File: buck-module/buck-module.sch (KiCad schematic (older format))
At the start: 10 parts, among them P1 CONN_01X04, P2 CONN_01X02, U1 ADP2301

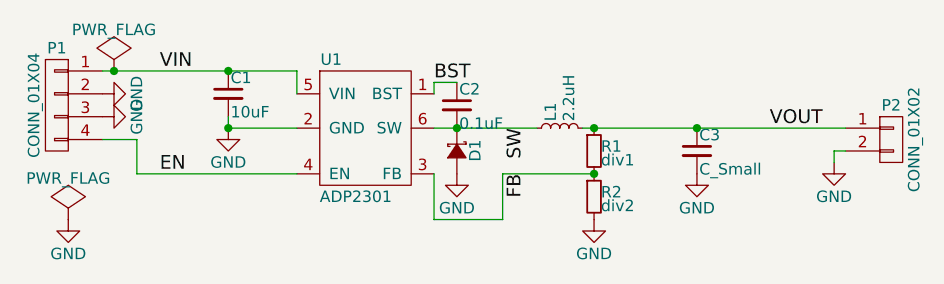
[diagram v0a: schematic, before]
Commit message: Fill in last details for power supply, cleanup
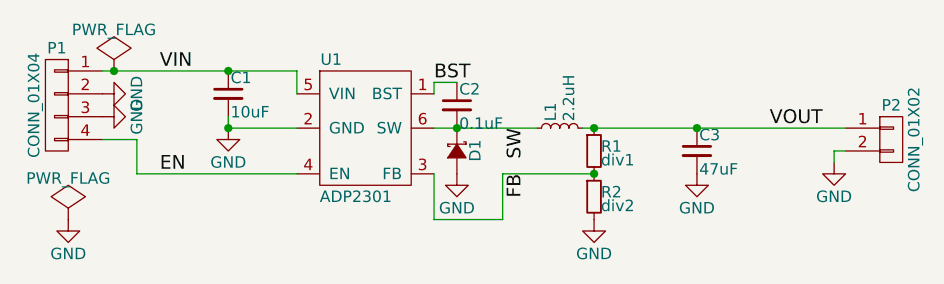
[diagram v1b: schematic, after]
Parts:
- C3: value C_Small -> 47uF
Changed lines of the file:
@@
 P 4800 3550
 F 0 "C3" H 4810 3620 50  0000 L CNN
-F 1 "C_Small" H 4810 3470 50  0000 L CNN
+F 1 "47uF" H 4810 3470 50  0000 L CNN
 F 2 "Capacitors_SMD:C_1210" H 4800 3550 50  0001 C CNN
 F 3 "" H 4800 3550 50  0000 C CNN
